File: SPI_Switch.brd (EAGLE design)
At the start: 100 x 80 mm, 40 parts, among them J1 8516-4500PL, J2 1-406525-1, J3 1-406525-1, J4 0705510037, J5 0705510037, U1 TLE7230G, U2 SN74ABT126

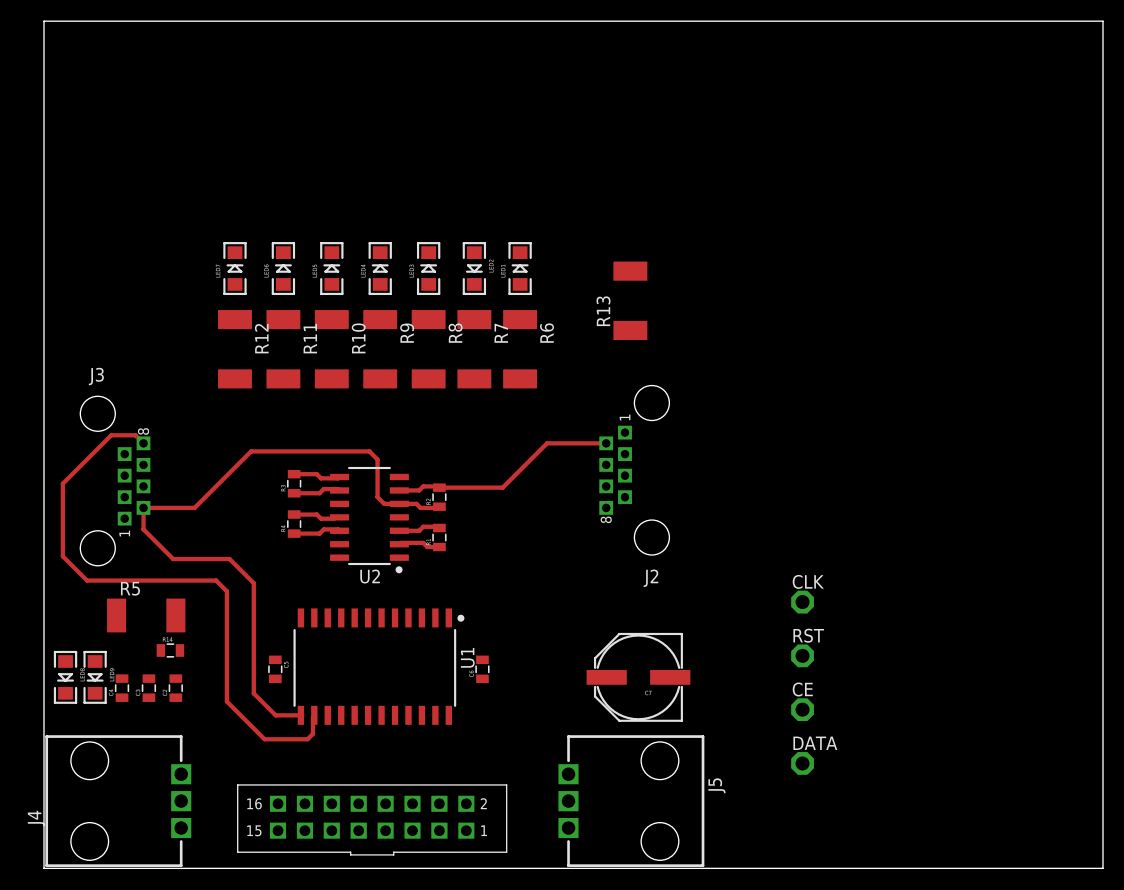
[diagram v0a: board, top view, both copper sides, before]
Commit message: Added channel routings
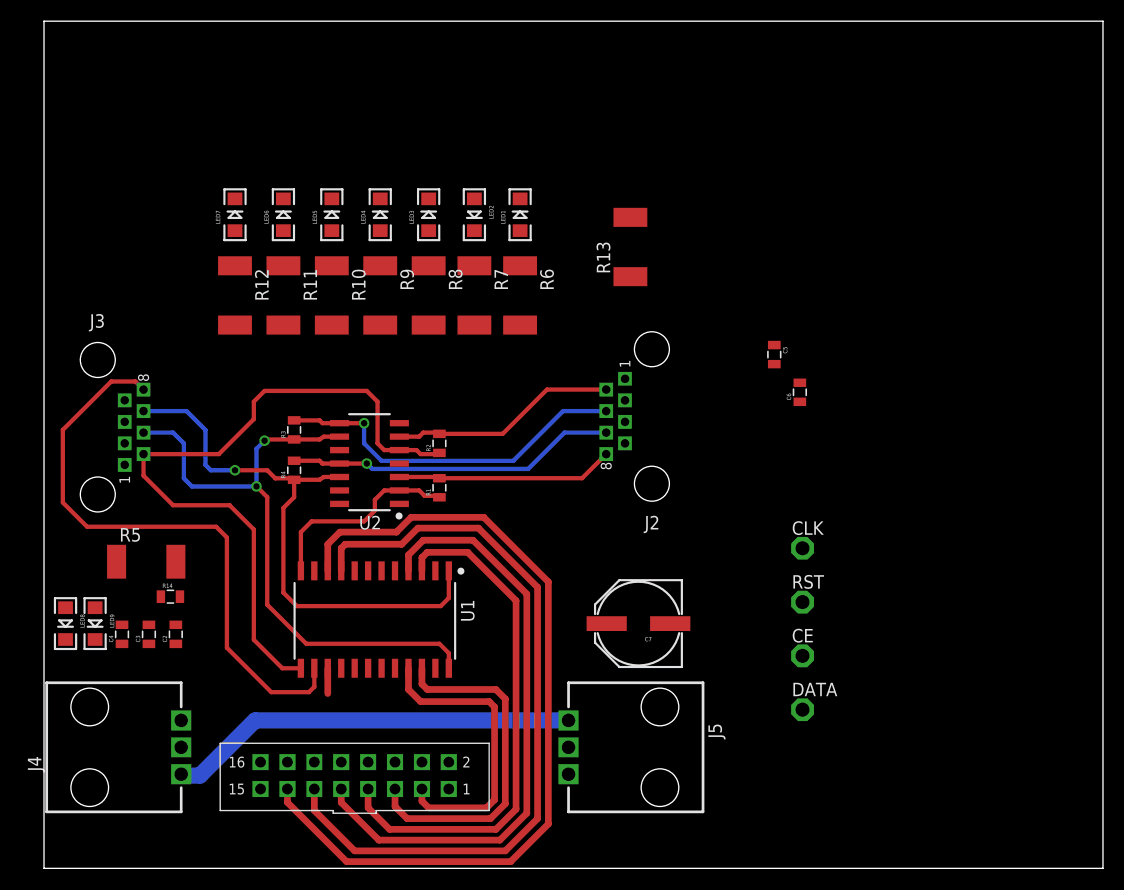
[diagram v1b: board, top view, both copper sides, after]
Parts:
- moved C5 55.7 mm to (69.0, 48.5)
- moved C6 39.8 mm to (71.4, 45.0)
- moved C7 5.08 mm to (56.1, 23.1)
- moved LED8 5.08 mm to (2.03, 23.1)
- moved LED9 5.08 mm to (4.83, 23.1)
- moved RST 5.08 mm to (71.6, 25.1)
- moved U2 5.08 mm to (34.8, 33.3)
- moved DATA 5.08 mm to (71.6, 15.0)
- moved J4 5.08 mm to (13.0, 8.89)
- moved J5 5.08 mm to (49.5, 14.0)
- moved C2 5.08 mm to (12.4, 22.1)
- moved C3 5.08 mm to (9.91, 22.1)
- moved C4 5.08 mm to (7.37, 22.1)
- moved CE 5.08 mm to (71.6, 20.1)
- moved CLK 5.08 mm to (71.6, 30.2)
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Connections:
- net CE: now also U1.1
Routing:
- net CH6: track 0.00 -> 79.5 mm
- net CH5: track 0.00 -> 71.6 mm
- net CH4: track 0.00 -> 57.4 mm
- net RST: track 4.50 -> 58.1 mm, vias 0 -> 2
- net CH3: track 0.00 -> 49.3 mm
- net CE: track 4.62 -> 53.4 mm, vias 0 -> 1
- net +24V: track 0.00 -> 38.8 mm
- net CH2: track 0.00 -> 33.0 mm
- net RST_POST: track 4.50 -> 34.1 mm, vias 0 -> 1
- net CH1: track 0.00 -> 28.2 mm
- net CE_POST: track 3.97 -> 30.6 mm, vias 0 -> 1
- net DATA_OUT_POST: track 3.99 -> 20.5 mm
- net DATA_OUT: track 4.00 -> 19.2 mm
- net CH7: track 0.00 -> 2.38 mm
- net CLK: track 64.8 -> 66.7 mm

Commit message: moved some parts to make layout for power cleaner
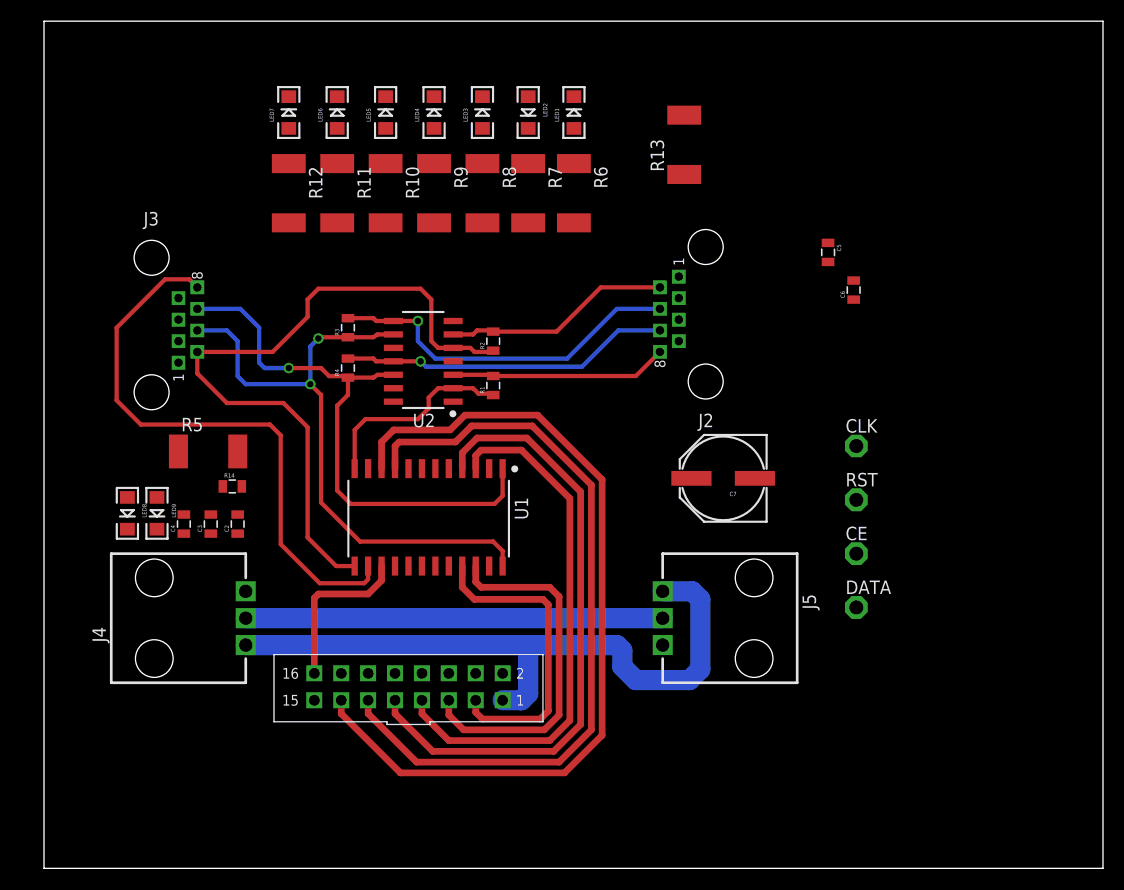
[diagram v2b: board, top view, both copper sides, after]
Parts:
- moved C7 15.9 mm to (64.1, 36.8)
- moved J5 15.1 mm to (58.4, 26.2)
- moved J4 13.6 mm to (19.1, 21.1)
- moved C2 11.9 mm to (18.3, 32.5)
- moved C3 11.9 mm to (15.7, 32.5)
- moved C4 11.9 mm to (13.2, 32.5)
- moved R14 11.9 mm to (17.8, 36.1)
- moved R5 11.9 mm to (15.5, 39.4)
- moved LED8 11.9 mm to (7.87, 33.5)
- moved LED9 11.9 mm to (10.7, 33.5)
- moved J2 10.9 mm to (59.9, 55.9)
- moved R10 10.9 mm to (32.3, 63.8)
- moved R12 10.9 mm to (23.1, 63.8)
- moved R3 10.9 mm to (28.7, 51.1)
- moved R4 10.9 mm to (28.7, 47.2)
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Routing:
- net +5V: track 0.00 -> 39.4 mm
- net +24V: track 38.8 -> 63.3 mm
- net CH7: track 2.38 -> 15.5 mm
- net CH6: track 79.5 -> 80.7 mm
- net CH4: track 57.4 -> 58.6 mm
- net CH1: track 28.2 -> 29.4 mm
- net CH2: track 33.0 -> 34.1 mm
- net CH3: track 49.3 -> 50.3 mm
- net DATA_IN: track 55.9 -> 55.0 mm
- net CH5: track 71.6 -> 72.4 mm

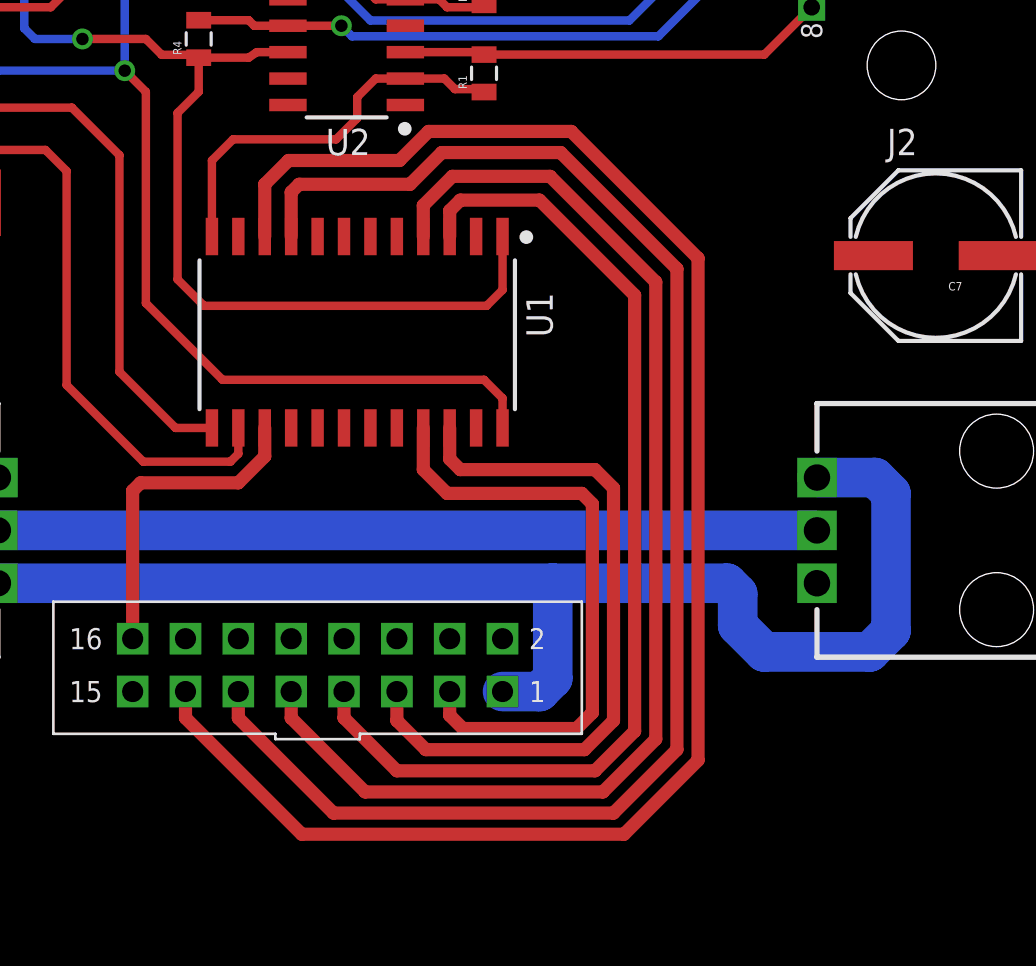
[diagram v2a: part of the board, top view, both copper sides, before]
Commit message: about to route lights. have lined up everything so that channels can easily be routed to LEDs
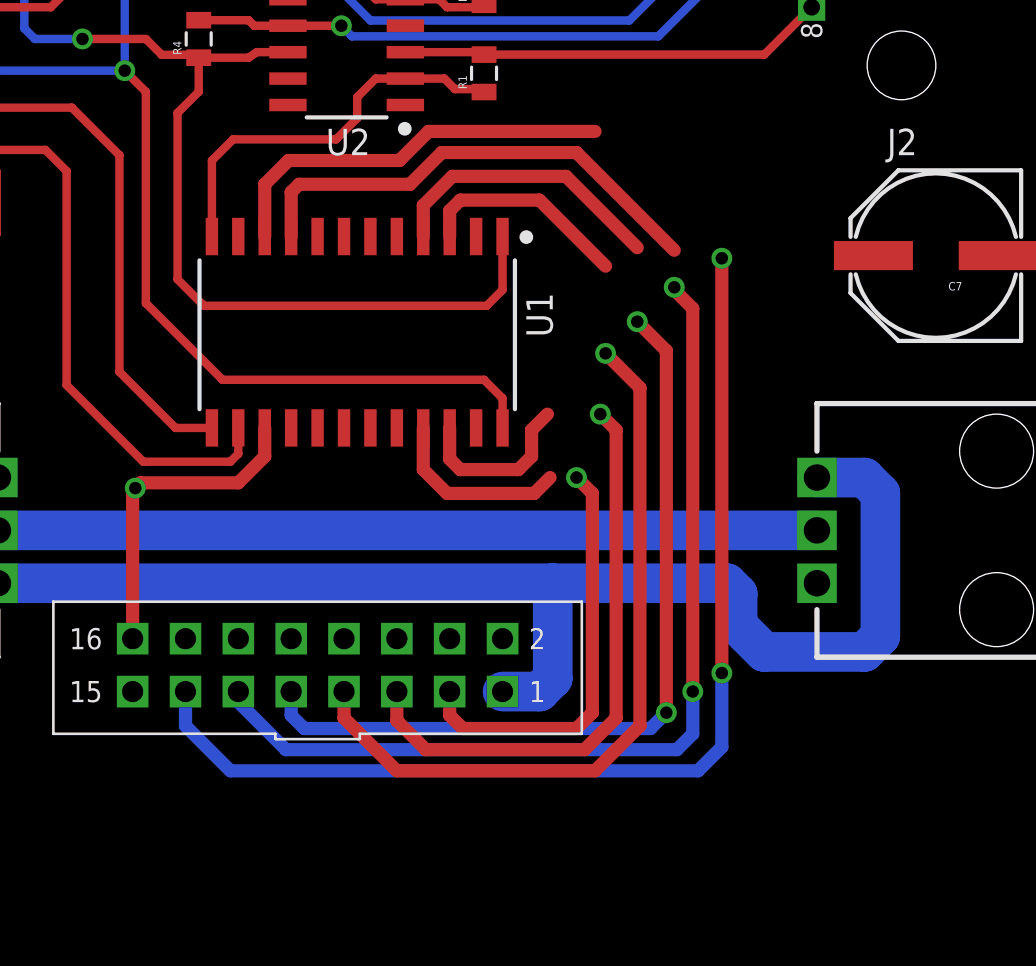
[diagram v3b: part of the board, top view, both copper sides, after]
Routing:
- net CH6: track 80.7 -> 71.7 mm, vias 0 -> 2
- net CH4: track 58.6 -> 52.9 mm, vias 0 -> 2
- net CH3: track 50.3 -> 46.3 mm, vias 0 -> 1
- net CH5: track 72.4 -> 68.7 mm, vias 0 -> 2
- net CH2: track 34.1 -> 36.3 mm, vias 0 -> 1
- net +24V: track 63.3 -> 62.5 mm
- net CH1: track 29.4 -> 29.1 mm, vias 0 -> 1
- net CH7: vias 0 -> 1

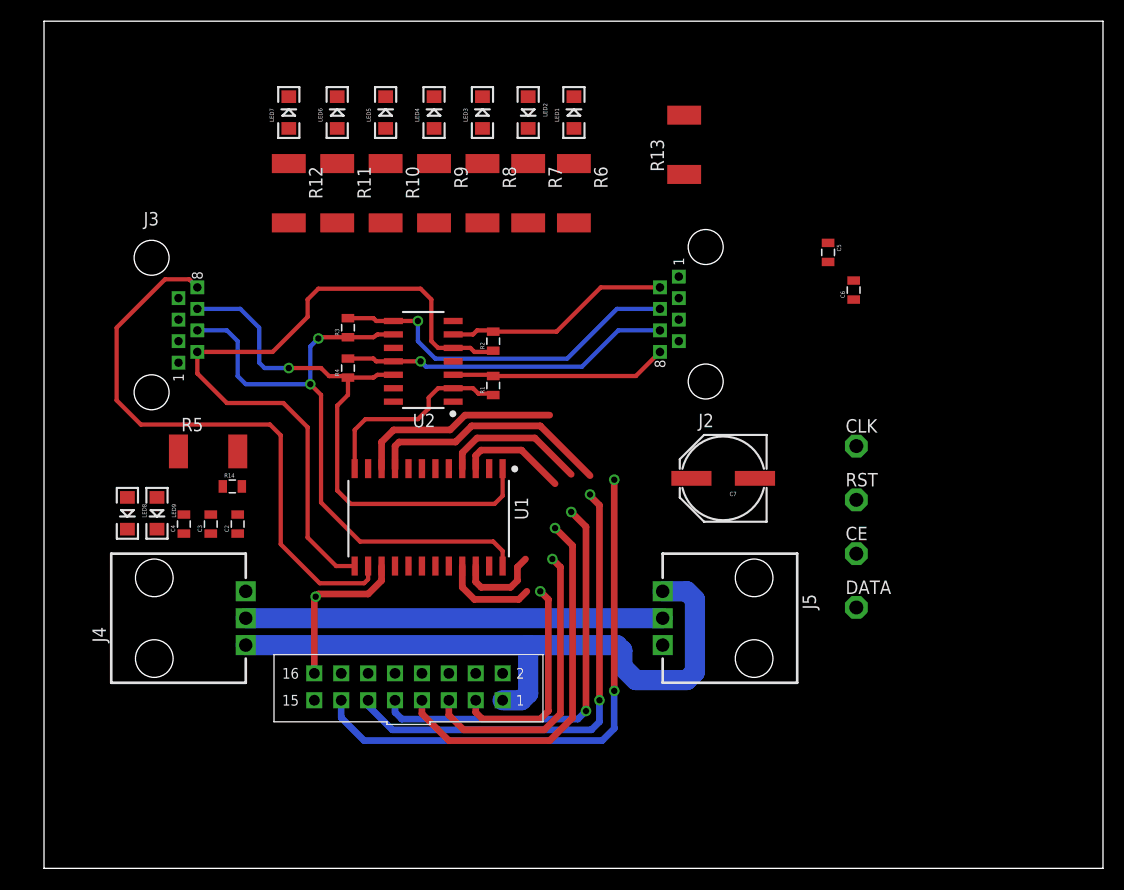
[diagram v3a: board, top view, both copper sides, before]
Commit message: finished fanning out LEDs
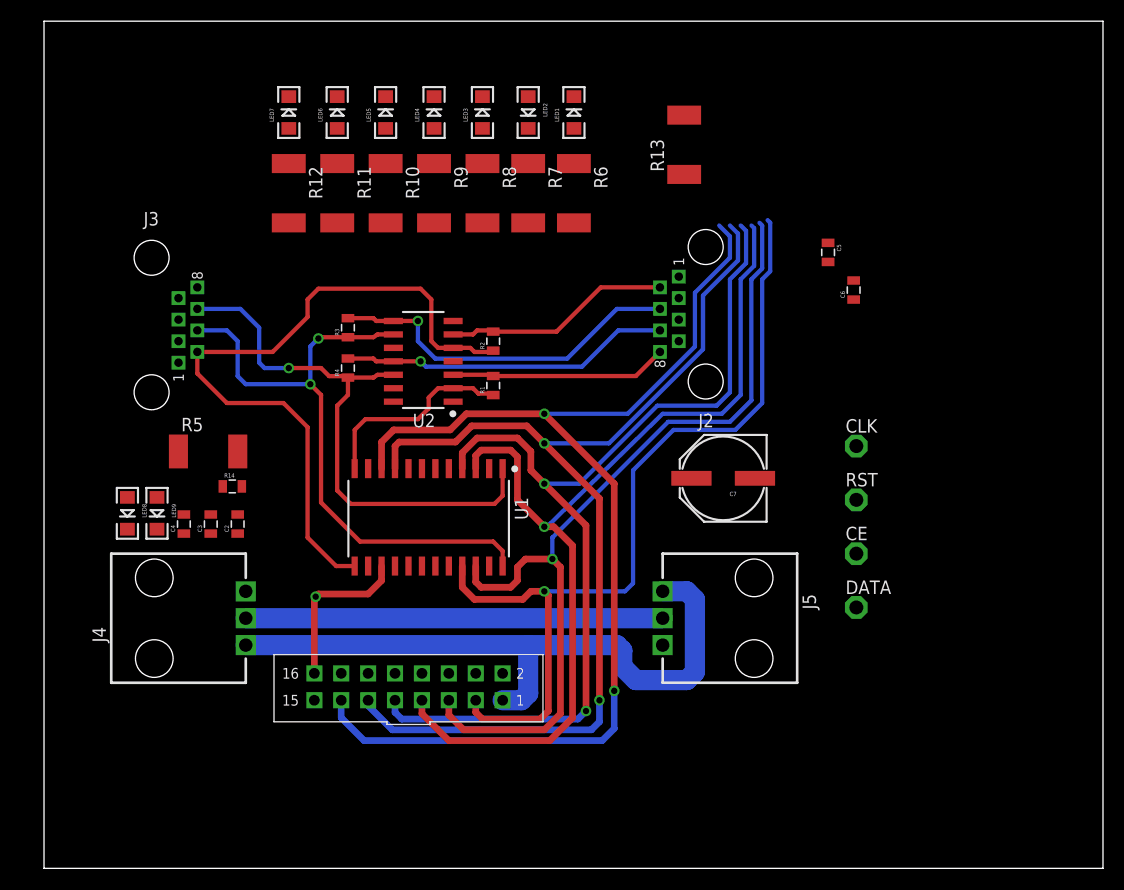
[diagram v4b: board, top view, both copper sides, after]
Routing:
- net DATA_IN: track 55.0 -> 0.00 mm
- net CH1: track 29.1 -> 82.5 mm
- net CH2: track 36.3 -> 82.3 mm
- net CH3: track 46.3 -> 90.7 mm
- net CH4: track 52.9 -> 93.2 mm
- net CH6: track 71.7 -> 110.3 mm
- net CH5: track 68.7 -> 101.8 mm

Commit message: finished routing except decoupling caps
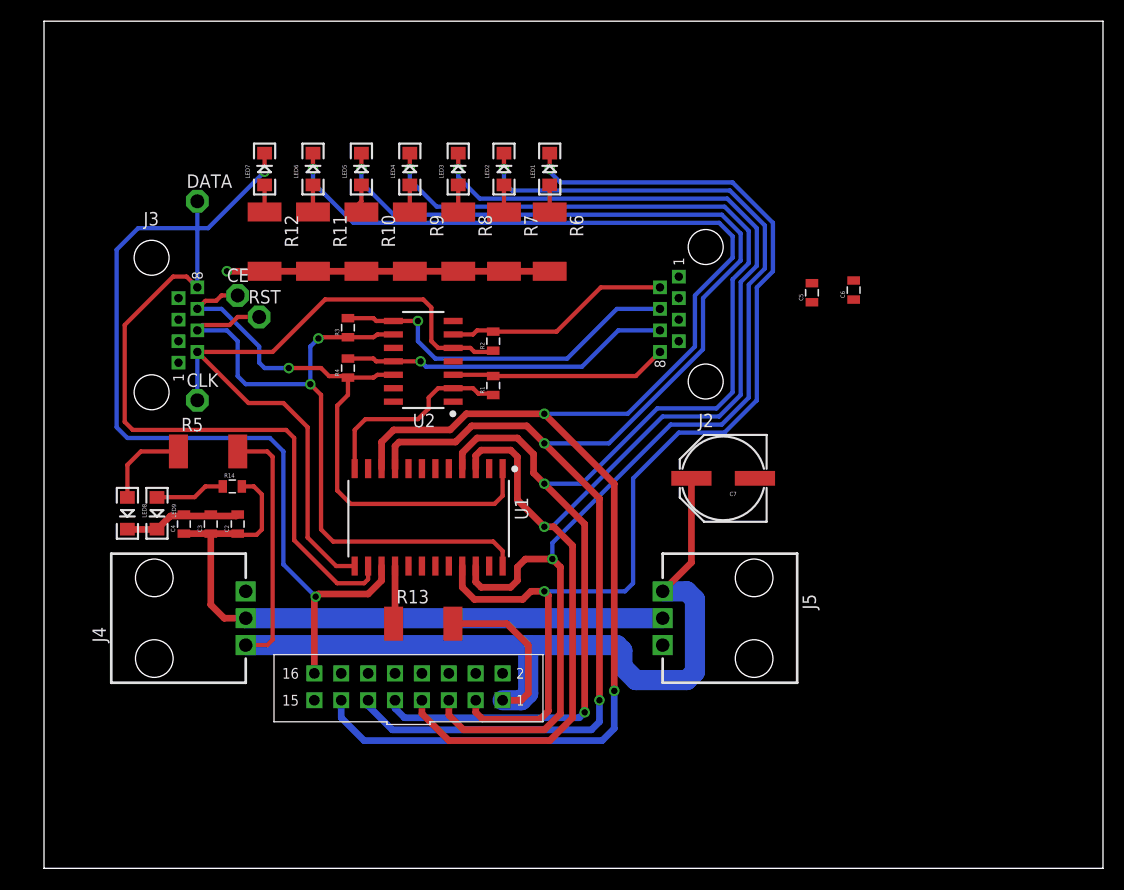
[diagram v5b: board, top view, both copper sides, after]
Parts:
- moved DATA 73.1 mm to (14.5, 63.0)
- moved CE 63.3 mm to (18.3, 54.1)
- moved CLK 62.4 mm to (14.5, 44.2)
- moved RST 59.0 mm to (20.3, 52.1)
- moved R13 51.5 mm to (35.8, 23.1), turned to 0 degrees
- moved LED2 5.80 mm to (43.4, 66.0), turned to 90 degrees
- moved LED3 5.80 mm to (39.1, 66.0)
- moved LED4 5.80 mm to (34.5, 66.0)
- moved LED5 5.80 mm to (30.0, 66.0)
- moved LED6 5.80 mm to (25.4, 66.0)
- moved LED7 5.80 mm to (20.8, 66.0)
- moved LED1 5.80 mm to (47.8, 66.0)
- moved R10 5.11 mm to (30.0, 59.2)
- moved R11 5.11 mm to (25.4, 59.2)
- moved R12 5.11 mm to (20.8, 59.2)
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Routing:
- net +24V: track 62.5 -> 143.5 mm, vias 0 -> 1
- net CH7: track 15.5 -> 82.7 mm, vias 1 -> 2
- net DATA_IN: track 0.00 -> 62.8 mm
- net CH6: track 110.3 -> 153.5 mm, vias 2 -> 3
- net CH5: track 101.8 -> 141.4 mm, vias 2 -> 3
- net CH4: track 93.2 -> 128.8 mm, vias 2 -> 3
- net CH3: track 90.7 -> 123.2 mm, vias 1 -> 2
- net CH2: track 82.3 -> 110.6 mm, vias 1 -> 2
- net CH1: track 82.5 -> 106.1 mm, vias 1 -> 2
- net +5V: track 39.4 -> 63.1 mm
- net GND: track 0.00 -> 11.0 mm
- net N$2: track 0.00 -> 8.42 mm
- net RST: track 58.1 -> 66.0 mm
- net N$4: track 0.00 -> 6.64 mm
- net CH8: track 0.00 -> 5.49 mm
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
